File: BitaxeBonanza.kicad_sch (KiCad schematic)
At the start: 12 parts, among them J1 XT30

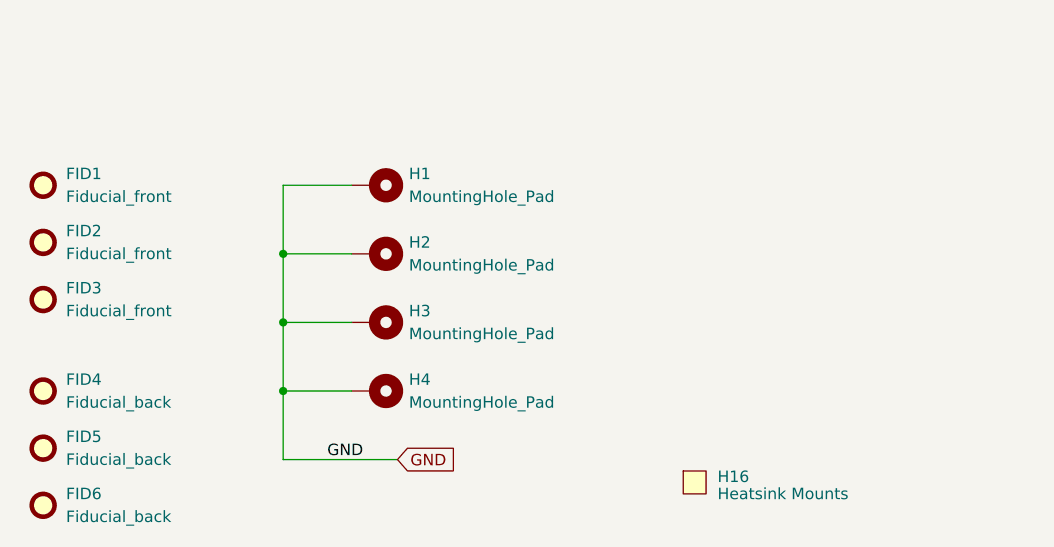
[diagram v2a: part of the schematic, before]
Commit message: moved ASIC bypass caps out to separate sheet
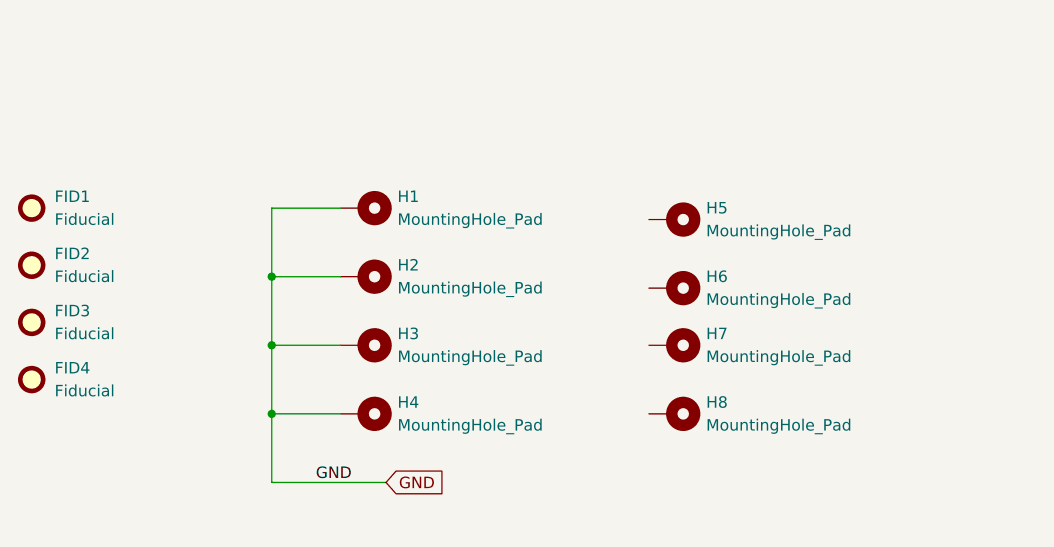
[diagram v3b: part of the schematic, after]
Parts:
- removed FID5, FID6: Fiducial_back, Fiducial:Fiducial_1mm_Mask2mm, symbol Mechanical:Fiducial
- removed H16: Heatsink Mounts, bitaxe:GT_heatsink, symbol bitaxe:gt_heatsink
- added H5, H6, H7, H8: MountingHole_Pad, bitaxe:Sinhoo SMTSO3015CTJ_nopaste, symbol Mechanical:MountingHole_Pad
- FID1, FID2, FID3: value Fiducial_front -> Fiducial; footprint Fiducial:Fiducial_1mm_Mask2mm -> bitaxe:Fiducial_1mm_Mask2mm
- FID4: value Fiducial_back -> Fiducial; footprint Fiducial:Fiducial_1mm_Mask2mm -> bitaxe:Fiducial_1mm_Mask2mm
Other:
- moved on the sheet: FID1, FID2, FID3, H1, H2, H3, H4

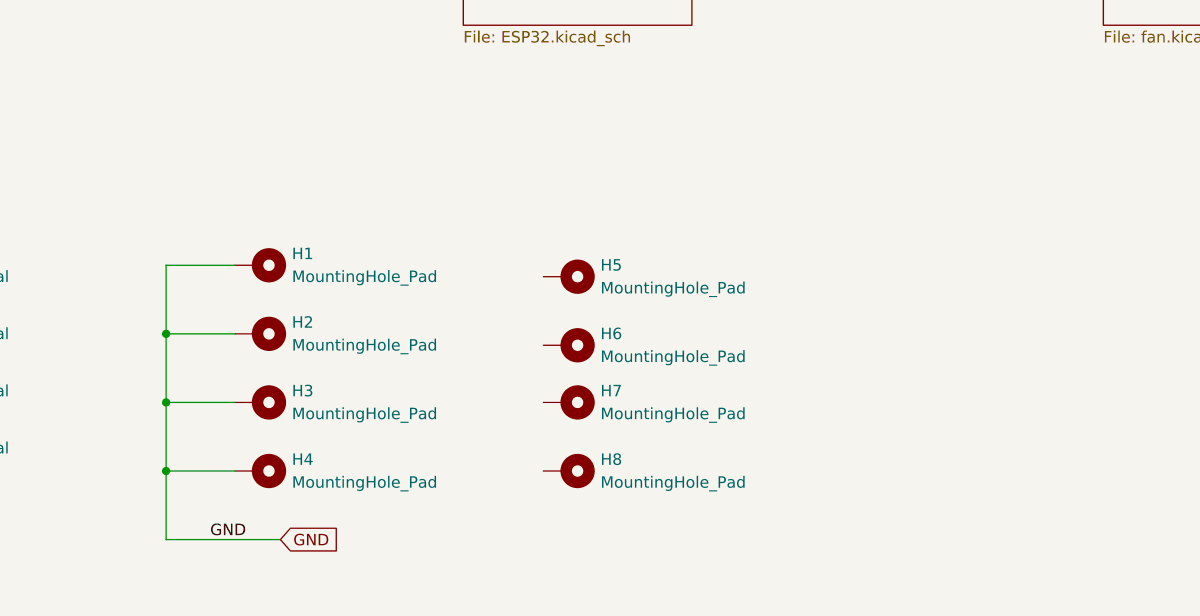
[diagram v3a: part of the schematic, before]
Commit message: made the board double wide. rough ASIC and vreg placement.
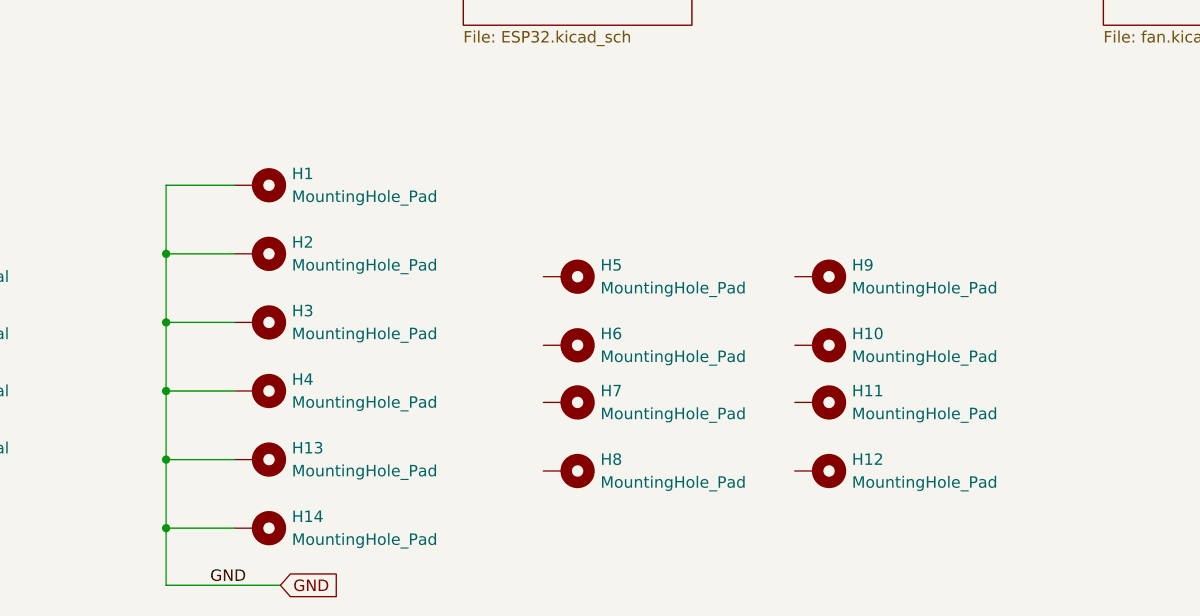
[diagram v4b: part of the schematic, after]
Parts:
- added H10, H11, H12, H9: MountingHole_Pad, bitaxe:Sinhoo SMTSO3015CTJ_nopaste, symbol Mechanical:MountingHole_Pad
- added H13, H14: MountingHole_Pad, MountingHole:MountingHole_3.2mm_M3_Pad_Via, symbol Mechanical:MountingHole_Pad
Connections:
- net GND: now also H13.1, H14.1
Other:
- moved on the sheet: H1, H2, H3, H4

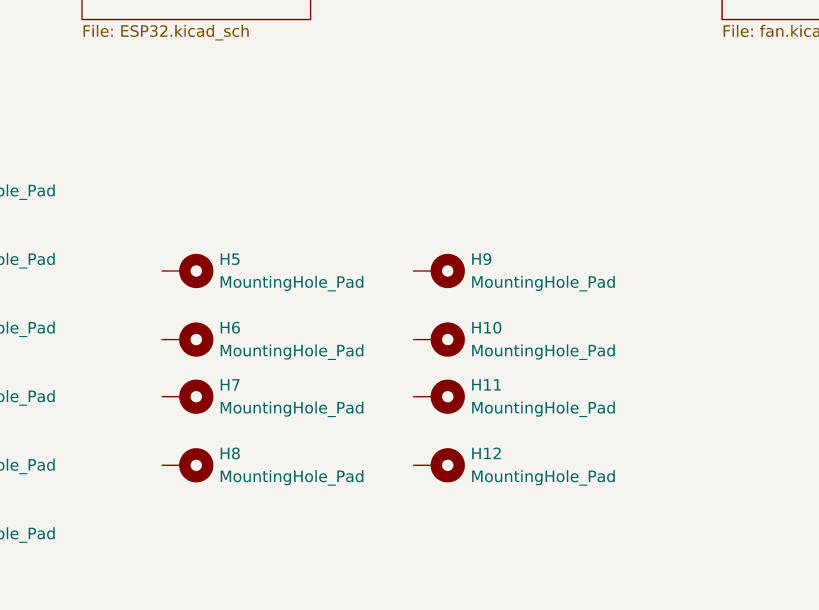
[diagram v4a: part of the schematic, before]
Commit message: ASICs placed. most other parts placed.
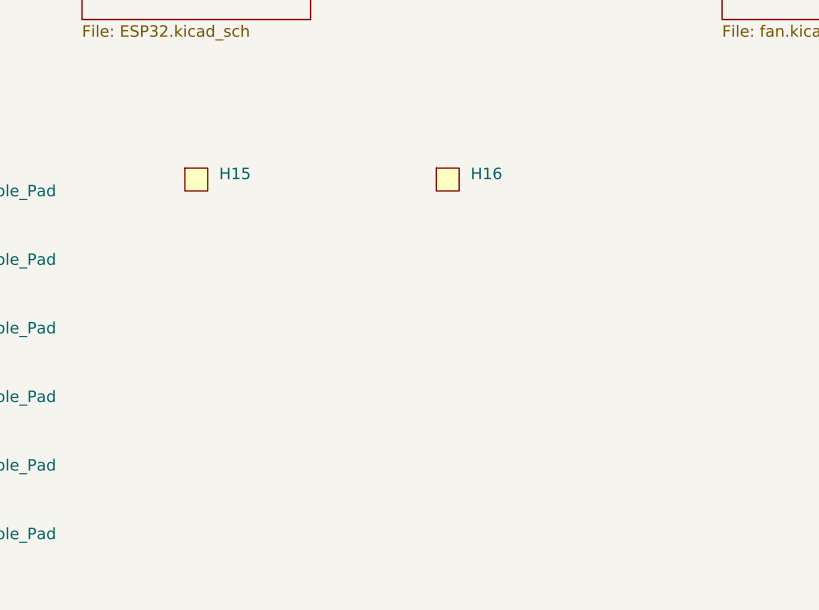
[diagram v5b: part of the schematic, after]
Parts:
- removed H10, H11, H12, H5, H6, H7, H8, H9: MountingHole_Pad, bitaxe:Sinhoo SMTSO3015CTJ_nopaste, symbol Mechanical:MountingHole_Pad
- added H15, H16: ~, bitaxe:bitaxeGT_extruded_heatsink, symbol bitaxe:gt_heatsink

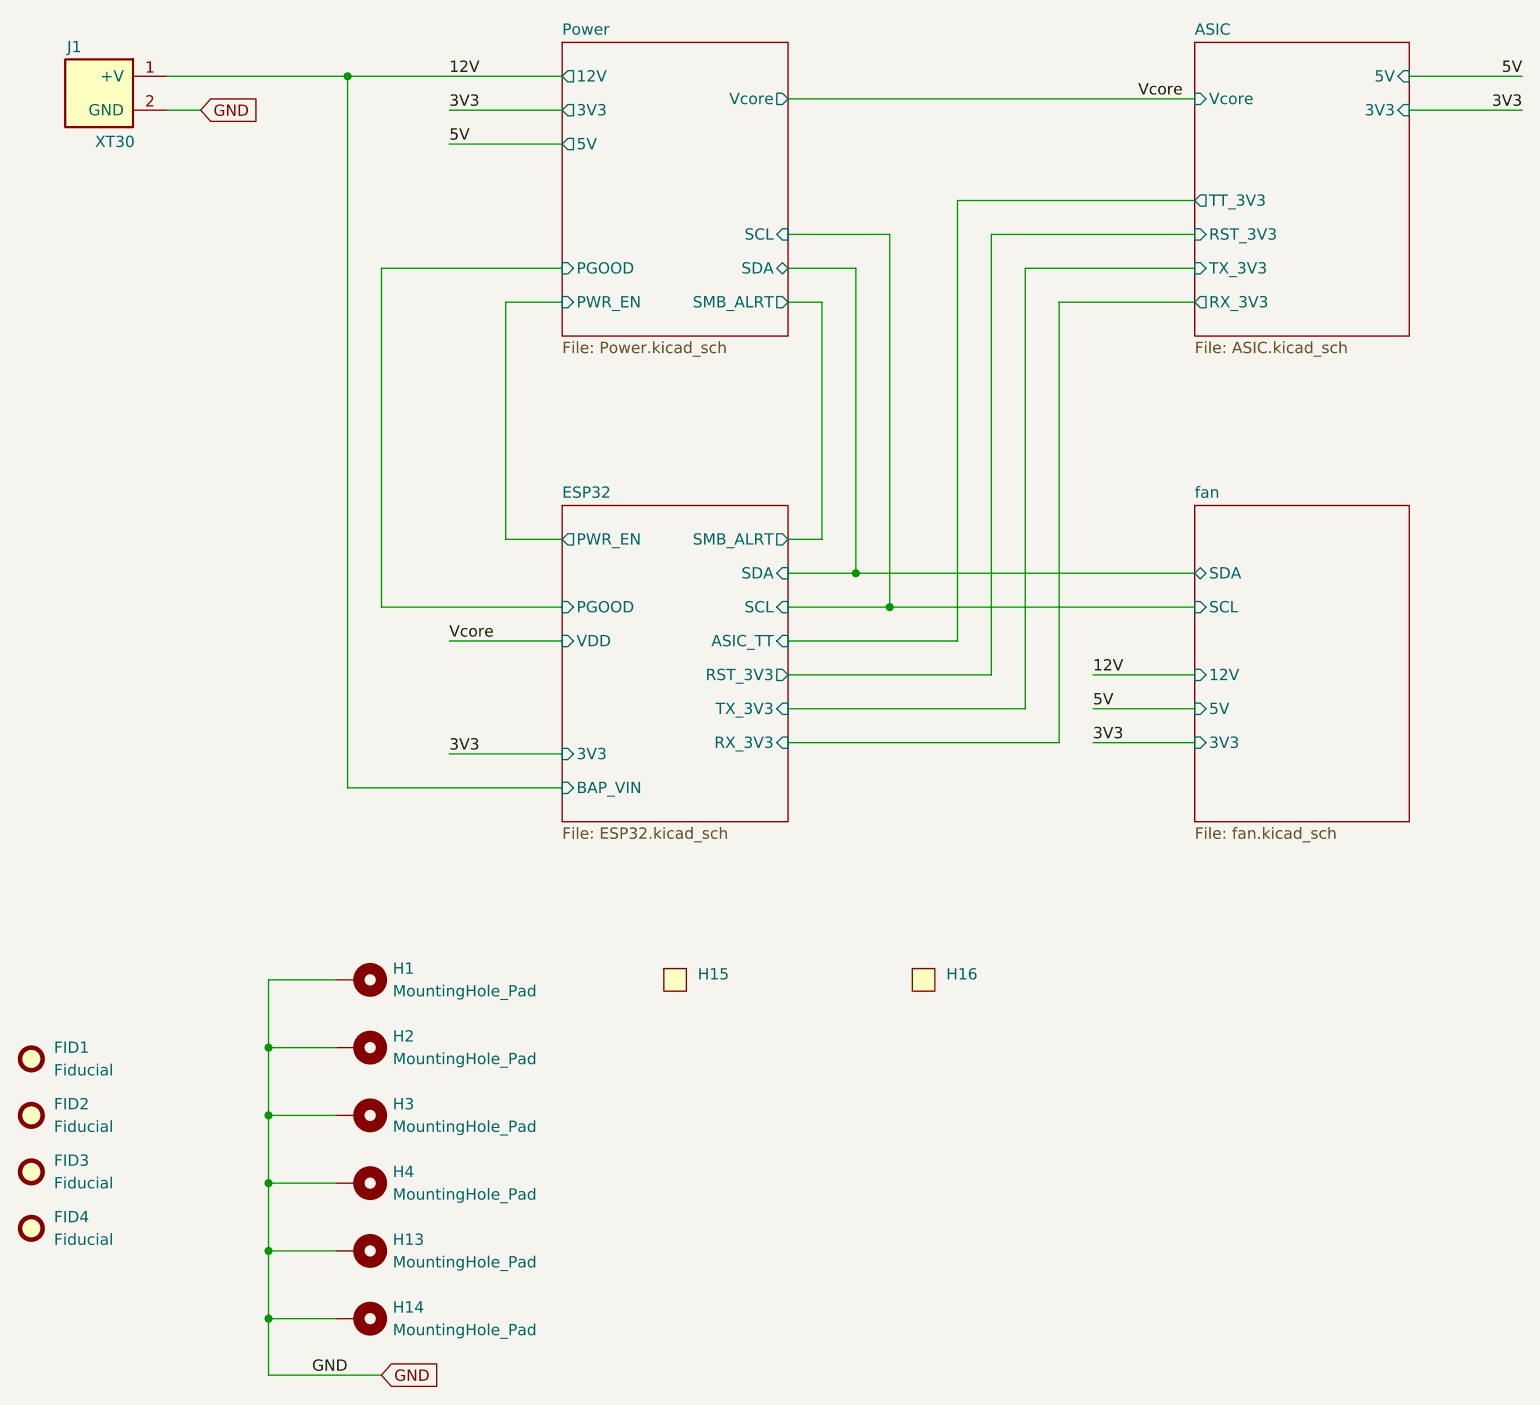
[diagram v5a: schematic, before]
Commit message: routing is done. Power planes look good. DRC pass
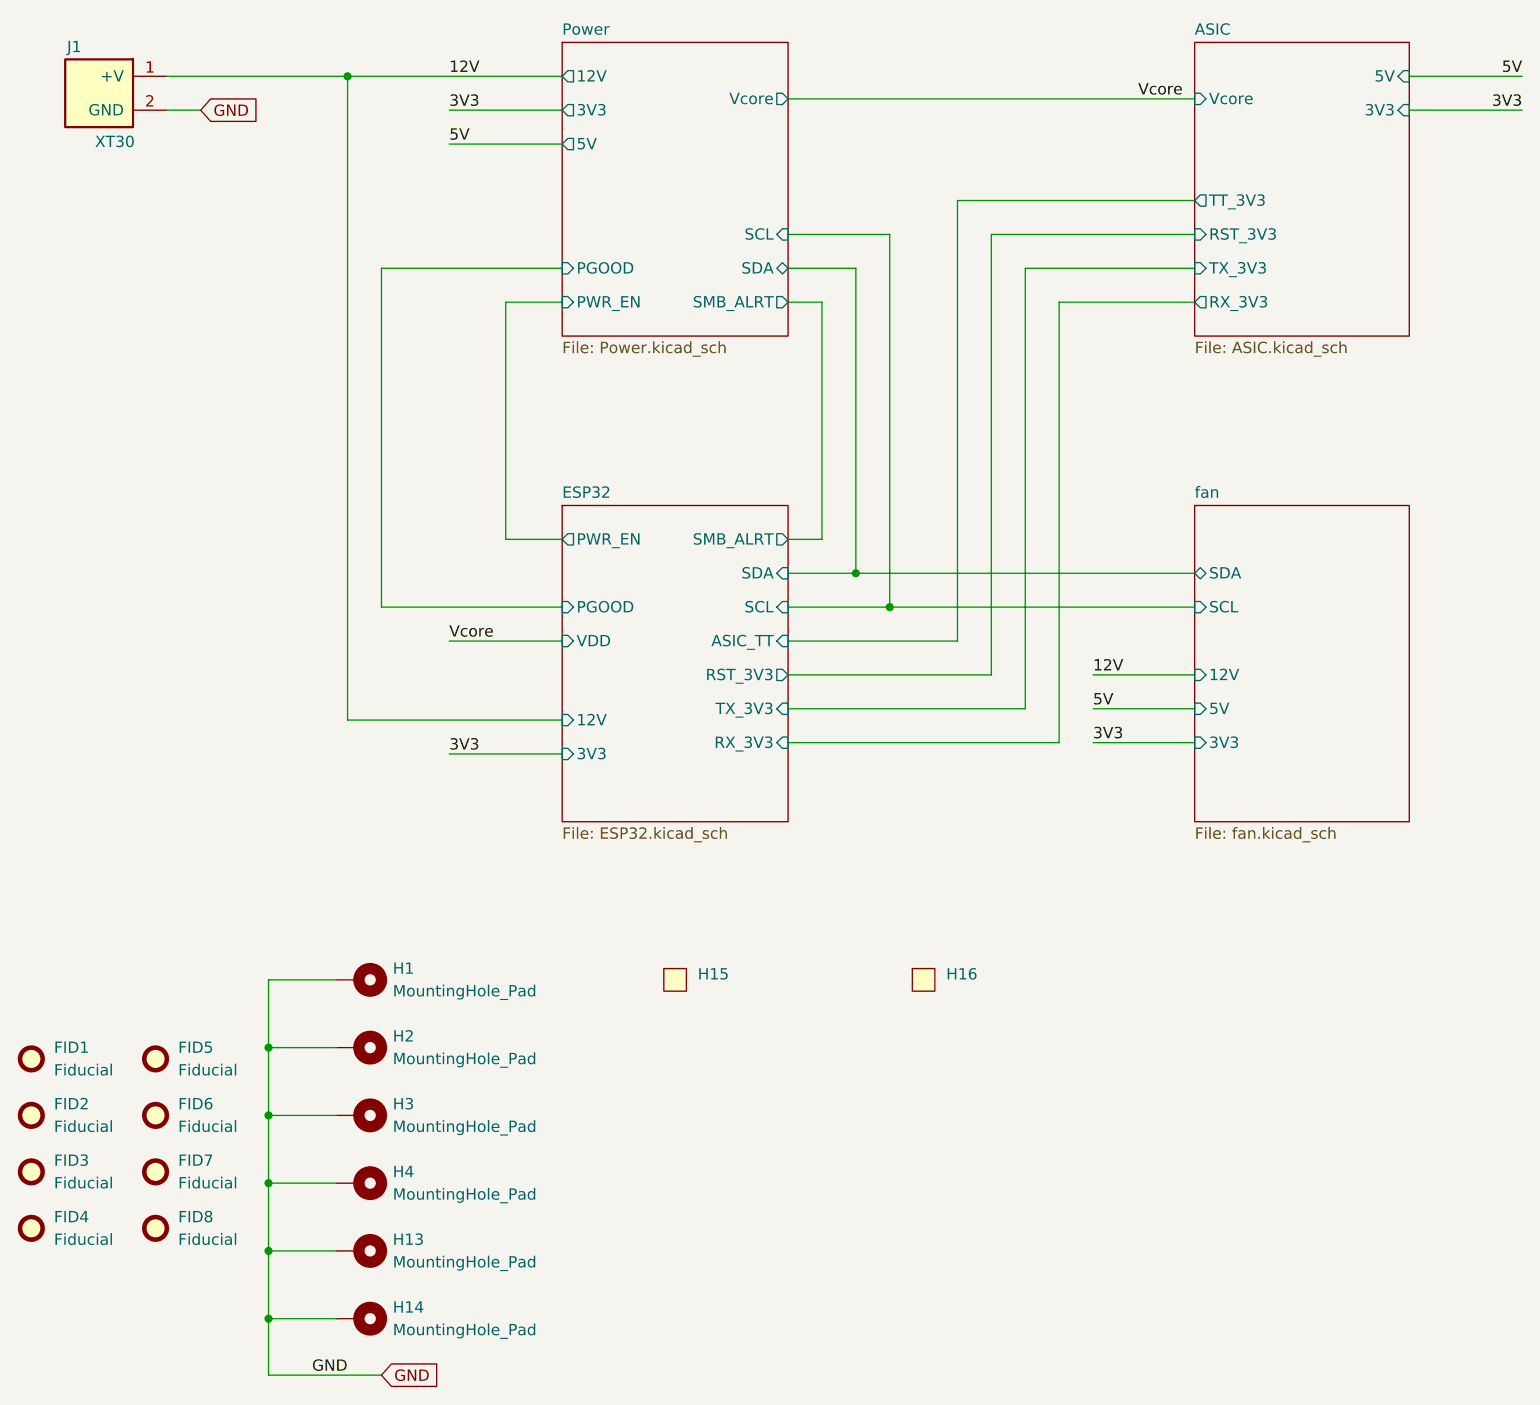
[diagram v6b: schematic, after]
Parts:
- added FID5, FID6, FID7, FID8: Fiducial, bitaxe:Fiducial_1mm_Mask2mm, symbol Mechanical:Fiducial
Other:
- sheet ESP32 ports: added 12V; removed BAP_VIN

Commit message: added gerbers and BOM
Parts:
- H15, H16: now left out of the parts list
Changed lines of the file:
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@@
 		(unit 1)
 		(exclude_from_sim no)
-		(in_bom yes)
+		(in_bom no)
 		(on_board yes)
 		(dnp no)
@@
 		(unit 1)
 		(exclude_from_sim no)
-		(in_bom yes)
-		(on_board yes)
-		(dnp no)
+		(in_bom no)
+		(on_board yes)
+		(dnp no)

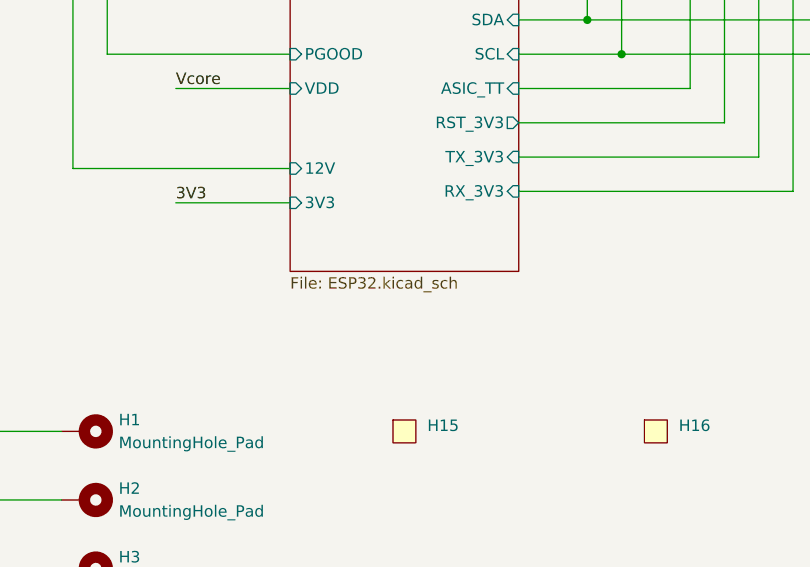
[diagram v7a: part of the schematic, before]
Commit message: changes esp32.kicad_sch case
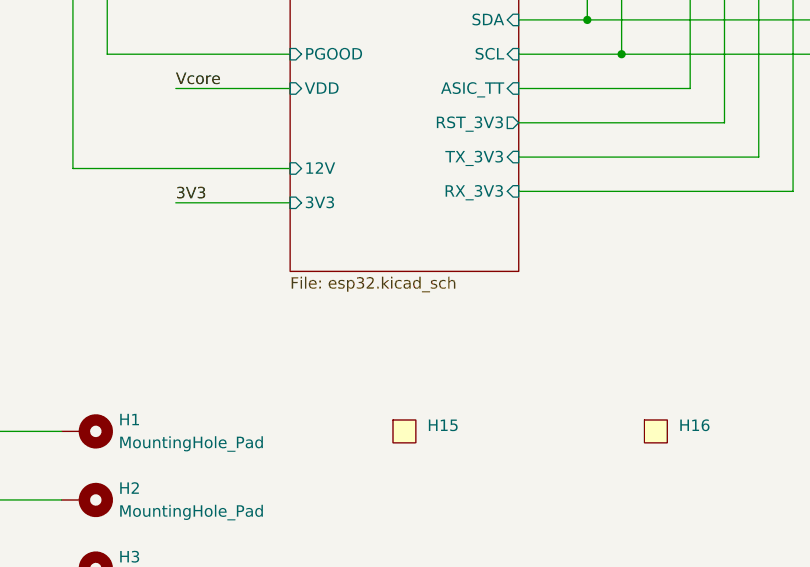
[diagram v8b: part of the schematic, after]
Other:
- sheet ESP32: file ESP32.kicad_sch -> esp32.kicad_sch
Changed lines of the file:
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@@
 			)
 		)
-		(property "Sheetfile" "ESP32.kicad_sch"
+		(property "Sheetfile" "esp32.kicad_sch"
 			(at 102.87 128.8546 0)
 			(effects
